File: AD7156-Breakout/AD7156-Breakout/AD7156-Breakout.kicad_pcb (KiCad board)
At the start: 2 copper layers, 13.2 x 15.7 mm, 5 parts, among them J1 Conn_01x06, J2 Cx1, J3 Cx2, U1 AD7156BCPZ-REEL7

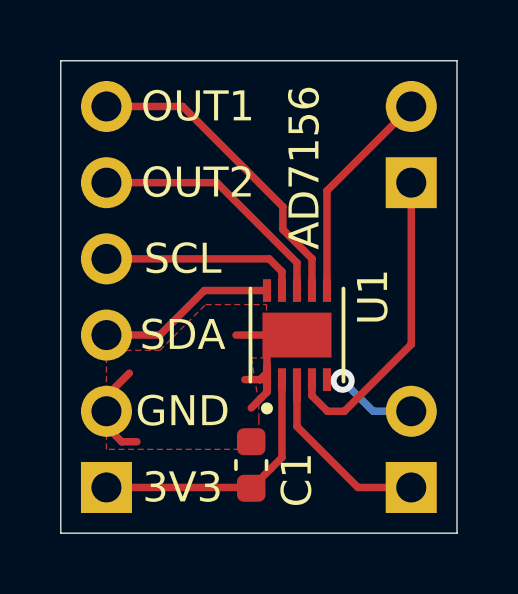
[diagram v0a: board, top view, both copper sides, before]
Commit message: Update AD7156
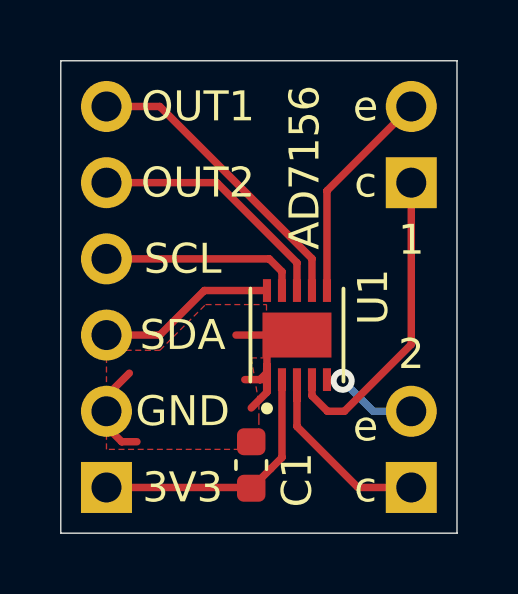
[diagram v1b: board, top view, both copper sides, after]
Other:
- net class Default removed
- board text added: "1"
- board text added: "2"
- board text added: "c"
- board text added: "e"
